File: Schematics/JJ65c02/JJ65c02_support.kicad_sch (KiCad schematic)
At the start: 40 parts, among them J1 ATMega J1, J2 Barrel_Jack, J3 VIA2 PortB, J4 ATMega J2, J6 AudioJack2, SW1 RESET, U2 NE555, U3 74HC00, U4 FT234XD, U5 74AC138, U6 LM386, U7 LM2940T-5.0/LF08, U8 ATmega328P-P, X1 1Mhz, X2 1.8Mhz, Y1 16Mhz

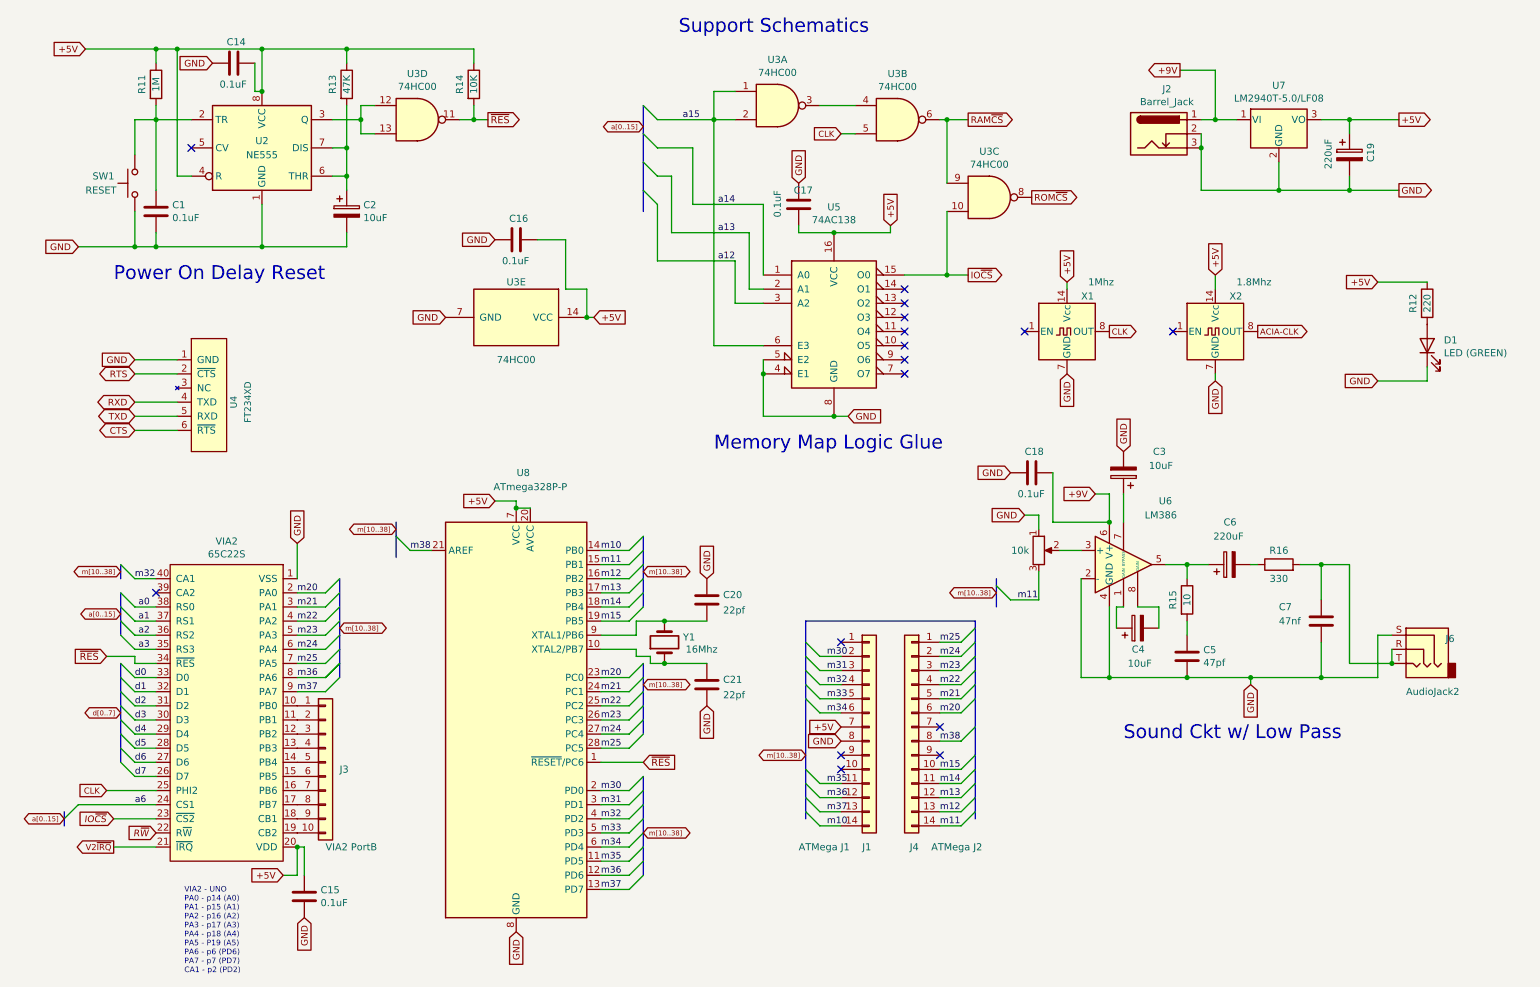
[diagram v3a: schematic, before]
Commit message: Refresh with current Schematics and wire-paths
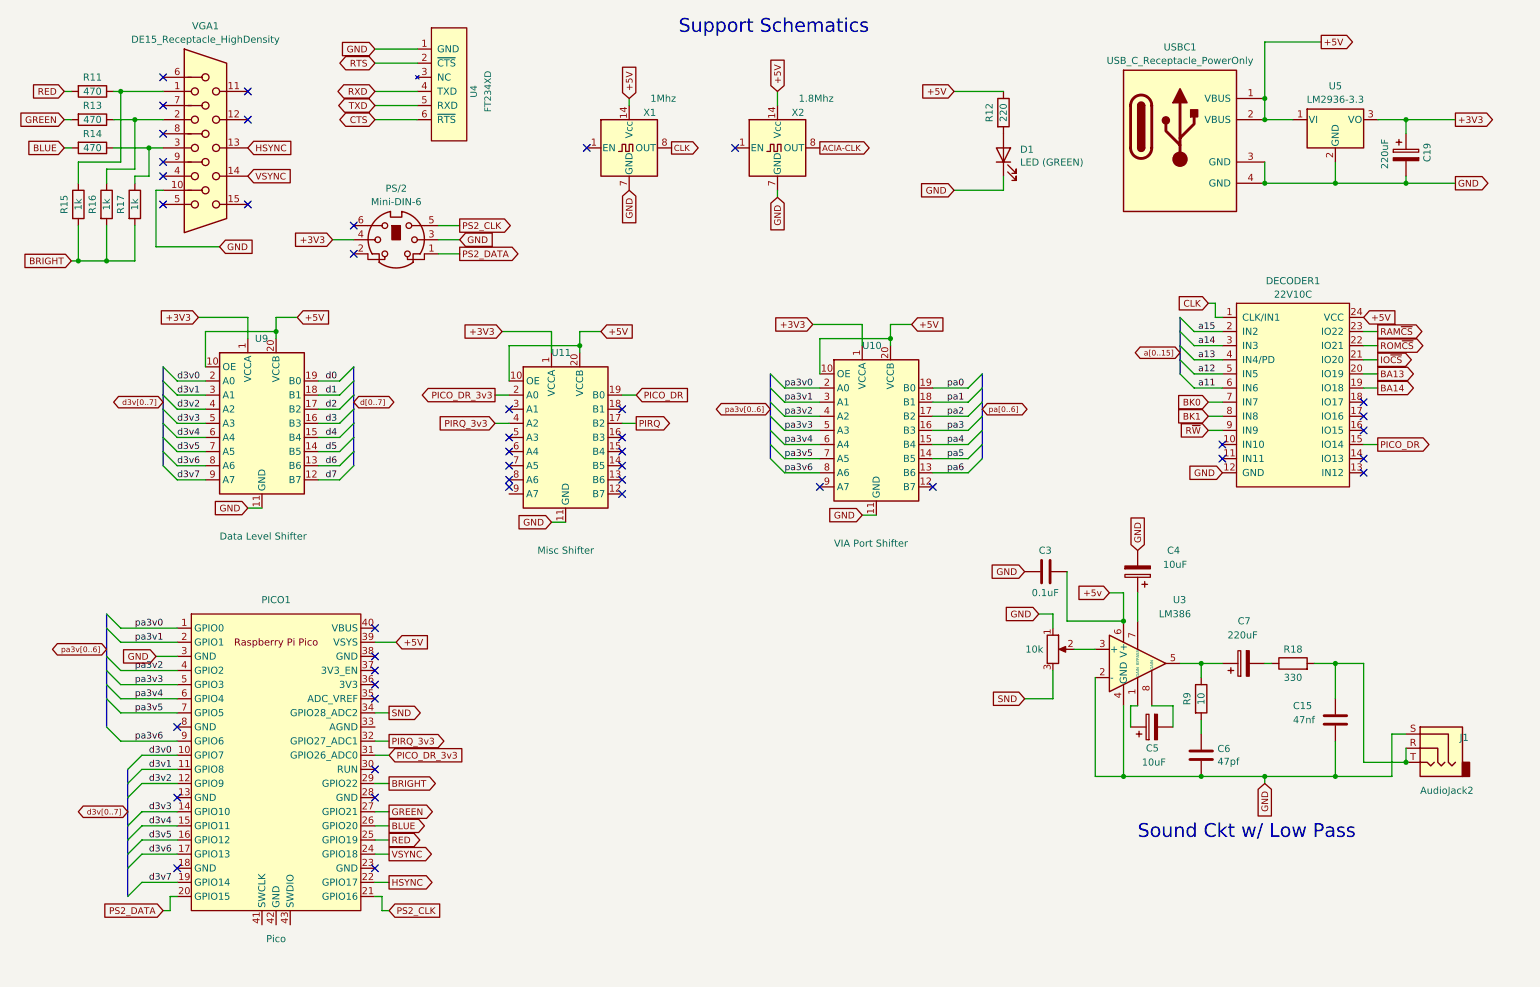
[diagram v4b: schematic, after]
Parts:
- removed C1, C14, C16, C17, C18: 0.1uF, Capacitor_THT:C_Disc_D4.7mm_W2.5mm_P5.00mm, symbol Device:C
- removed C2, C3: 10uF, Capacitor_THT:CP_Radial_D5.0mm_P2.50mm, symbol Device:C_Polarized
- removed C20, C21: 22pf, Capacitor_THT:C_Disc_D4.7mm_W2.5mm_P5.00mm, symbol Device:C
- removed C5: 47pf, Capacitor_THT:C_Disc_D4.7mm_W2.5mm_P5.00mm, symbol Device:C
- removed C6: 220uF, Capacitor_THT:CP_Radial_D6.3mm_P2.50mm, symbol Device:C_Polarized
- removed C7: 47nf, Capacitor_THT:C_Disc_D4.7mm_W2.5mm_P5.00mm, symbol Device:C
- removed J1: ATMega J1, Connector_PinHeader_2.54mm:PinHeader_1x14_P2.54mm_Vertical, symbol Connector_Generic:Conn_01x14
- removed J2: Barrel_Jack, Connector_BarrelJack:BarrelJack_Horizontal, symbol Connector:Barrel_Jack_Switch_Pin3Ring
- removed J3: VIA2 PortB, Connector_PinHeader_2.54mm:PinHeader_1x10_P2.54mm_Vertical, symbol Connector_Generic:Conn_01x10
- removed J4: ATMega J2, Connector_PinHeader_2.54mm:PinHeader_1x14_P2.54mm_Vertical, symbol Connector_Generic:Conn_01x14
- removed J6: AudioJack2, Connector_Audio:Jack_3.5mm_CUI_SJ1-3533NG_Horizontal, symbol Connector:AudioJack3
- removed RV2: 10k, Potentiometer_THT:Potentiometer_Bourns_3339P_Vertical, symbol Device:R_Potentiometer
- removed SW1: RESET, Button_Switch_THT:SW_PUSH_6mm, symbol Switch:SW_Push
- removed U2: NE555, Package_DIP:DIP-8_W7.62mm_Socket, symbol Timer:LM555xN
- removed U3: 74HC00, Package_DIP:DIP-14_W7.62mm_Socket, symbol 74xx:74HC00
- removed U5: 74AC138, Package_DIP:DIP-16_W7.62mm_Socket, symbol 74xx:74LS138
- removed U6: LM386, Package_DIP:DIP-8_W7.62mm_Socket, symbol Amplifier_Audio:LM386
- removed U7: LM2940T-5.0/LF08, Package_TO_SOT_THT:TO-262-3_Vertical, symbol JJ65c02-rescue:LM2940
- removed U8: ATmega328P-P, Package_DIP:DIP-28_W7.62mm_Socket, symbol MCU_Microchip_ATmega:ATmega328P-P
- removed VIA2: 65C22S, Package_DIP:DIP-40_W15.24mm_Socket, symbol 6502:65C22S
- removed Y1: 16Mhz, Crystal:Crystal_HC18-U_Vertical, symbol Device:Crystal
- added C3: 0.1uF, Capacitor_THT:C_Disc_D4.7mm_W2.5mm_P5.00mm, symbol Device:C
- added C5: 10uF, Capacitor_THT:CP_Radial_D5.0mm_P2.50mm, symbol Device:C_Polarized
- added C6: 47pf, Capacitor_THT:C_Disc_D4.7mm_W2.5mm_P5.00mm, symbol Device:C
- added C7: 220uF, Capacitor_THT:CP_Radial_D6.3mm_P2.50mm, symbol Device:C_Polarized
- added DECODER1: 22V10C, Package_DIP:DIP-24_W7.62mm_Socket, symbol 6502:22V10C
- added J1: AudioJack2, Connector_Audio:Jack_3.5mm_CUI_SJ1-3533NG_Horizontal, symbol Connector:AudioJack3
- added PICO1: Pico, JJ65c02:RPi_Pico_SMD_TH, symbol JJ65c02-rescue:Pico
- added PS/2: Mini-DIN-6, JJ65c02:mini_din-6, symbol Connector:Mini-DIN-6
- added R17: 1k, Resistor_THT:R_Axial_DIN0207_L6.3mm_D2.5mm_P7.62mm_Horizontal, symbol Device:R
- added R18: 330, Resistor_THT:R_Axial_DIN0207_L6.3mm_D2.5mm_P7.62mm_Horizontal, symbol Device:R
- added R9: 10, Resistor_THT:R_Axial_DIN0207_L6.3mm_D2.5mm_P7.62mm_Horizontal, symbol Device:R
- added RV1: 10k, Potentiometer_THT:Potentiometer_Bourns_3339P_Vertical, symbol Device:R_Potentiometer
- added U10: VIA Port Shifter, JJ65c02:TXB0108, symbol JJ65c02-rescue:FXMA108
- added U11: Misc Shifter, JJ65c02:TXB0108, symbol JJ65c02-rescue:FXMA108
- added U3: LM386, Package_DIP:DIP-8_W7.62mm_Socket, symbol Amplifier_Audio:LM386
- added U5: LM2936-3.3, Package_TO_SOT_THT:TO-220-3_Vertical, symbol Regulator_Linear:LM2936-3.3
- added U9: Data Level Shifter, JJ65c02:TXB0108, symbol JJ65c02-rescue:FXMA108
- added USBC1: USB_C_Receptacle_PowerOnly, JJ65c02:USBC_power, symbol Connector:USB_C_Receptacle_PowerOnly_6P
- added VGA1: DE15_Receptacle_HighDensity, JJ65c02:CONN_HDE15P_AMP, symbol Connector:DE15_Receptacle_HighDensity
- C15: value 0.1uF -> 47nf
- R11: value 1M -> 470
- R13: value 47K -> 470
- R14: value 10K -> 470
- R15: value 10 -> 1k
- R16: value 330 -> 1k
- U4: footprint JJ65c02:maxboard -> TerminalBlock_TE-Connectivity:TerminalBlock_TE_282834-6_1x06_P2.54mm_Horizontal
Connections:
- net +5V: now also DECODER1.24 (VCC), PICO1.39 (VSYS), U10.10 (OE), U10.20 (VCCB), U11.10 (OE), U11.20 (VCCB), U5.1 (VI), U9.10 (OE), U9.20 (VCCB), USBC1.1 (VBUS), USBC1.2 (VBUS); no longer C15.1, C19.1, R11.1, R13.1, R14.1
- net CLK: now also DECODER1.1 (CLK/IN1)
- net GND: now also C4.2, C3.2, C6.2, DECODER1.12 (GND), J1.S, PICO1.3 (GND), PS/2.3, RV1.1, U10.11 (GND), U11.11 (GND), U3.2 (-), U3.4 (GND), U5.2 (GND), U9.11 (GND), USBC1.3 (GND), USBC1.4 (GND), VGA1.10
- net IO~{CS}: now also DECODER1.21 (IO20)
- net RAM~{CS}: now also DECODER1.23 (IO22)
- net ROM~{CS}: now also DECODER1.22 (IO21)
- net R~{W}: now also DECODER1.9 (IN9)
- net a12: now also DECODER1.5 (IN5)
- net a13: now also DECODER1.4 (IN4/PD)
- net a14: now also DECODER1.3 (IN3)
- net a15: now also DECODER1.2 (IN2)
- net d0: now also U9.19 (B0)
- net d1: now also U9.18 (B1)
- net d2: now also U9.17 (B2)
- net d3: now also U9.16 (B3)
- net d4: now also U9.15 (B4)
- net d5: now also U9.14 (B5)
- net d6: now also U9.13 (B6)
- net d7: now also U9.12 (B7)
- net RED: now reaches R11.2
- net RED: now also PICO1.25 (GPIO19)
- net GREEN: now reaches R13.2
- net GREEN: now also PICO1.27 (GPIO21)
- net at R16.1: now also R13.1, VGA1.2
- net BRIGHT: now reaches R16.2
- net BRIGHT: now also R15.2, PICO1.29 (GPIO22), R17.2
- net at C4.1: now also U3.7 (BYPASS)
- net at R15.1: now also R11.1, VGA1.1
- net ~{RES} renamed BLUE
- net BLUE: now also PICO1.26 (GPIO20)
- new net: C7.2, R18.1
- new net: C15.1, J1.R, J1.T, R18.2
- new net: C6.1, R9.2
- new net: R14.1, R17.1, VGA1.3
- new net: C5.1, U3.1 (GAIN)
- new net: RV1.2, U3.3 (+)
- new net: C7.1, R9.1, U3.5
- new net: C5.2, U3.8 (GAIN)
- new net +3V3: C19.1, PS/2.4, U10.1 (VCCA), U11.1 (VCCA), U5.3 (VO), U9.1 (VCCA)
- new net +5v: C3.1, U3.6 (V+)
- new net BA13: DECODER1.20 (IO19)
- new net BA14: DECODER1.19 (IO18)
- new net BK0: DECODER1.7 (IN7)
- new net BK1: DECODER1.8 (IN8)
- new net HSYNC: PICO1.22 (GPIO17), VGA1.13
- new net PICO_DR: DECODER1.15 (IO14), U11.19 (B0)
- new net PICO_DR_3v3: PICO1.31 (GPIO26_ADC0), U11.2 (A0)
- new net PIRQ: U11.17 (B2)
- new net PIRQ_3v3: PICO1.32 (GPIO27_ADC1), U11.4 (A2)
- new net PS2_CLK: PICO1.21 (GPIO16), PS/2.5
- new net PS2_DATA: PICO1.20 (GPIO15), PS/2.1
- new net SND: PICO1.34 (GPIO28_ADC2), RV1.3
- new net VSYNC: PICO1.24 (GPIO18), VGA1.14
- new net a11: DECODER1.6 (IN6)
- new net d3v0: PICO1.10 (GPIO7), U9.2 (A0)
- new net d3v1: PICO1.11 (GPIO8), U9.3 (A1)
- new net d3v2: PICO1.12 (GPIO9), U9.4 (A2)
- new net d3v3: PICO1.14 (GPIO10), U9.5 (A3)
- new net d3v4: PICO1.15 (GPIO11), U9.6 (A4)
- new net d3v5: PICO1.16 (GPIO12), U9.7 (A5)
- new net d3v6: PICO1.17 (GPIO13), U9.8 (A6)
- new net d3v7: PICO1.19 (GPIO14), U9.9 (A7)
- new net pa0: U10.19 (B0)
- new net pa1: U10.18 (B1)
- new net pa2: U10.17 (B2)
- new net pa3: U10.16 (B3)
- new net pa3v0: PICO1.1 (GPIO0), U10.2 (A0)
- new net pa3v1: PICO1.2 (GPIO1), U10.3 (A1)
- new net pa3v2: PICO1.4 (GPIO2), U10.4 (A2)
- new net pa3v3: PICO1.5 (GPIO3), U10.5 (A3)
- new net pa3v4: PICO1.6 (GPIO4), U10.6 (A4)
- new net pa3v5: PICO1.7 (GPIO5), U10.7 (A5)
- new net pa3v6: PICO1.9 (GPIO6), U10.8 (A6)
- new net pa4: U10.15 (B4)
- new net pa5: U10.14 (B5)
- new net pa6: U10.13 (B6)
- no-connect marks 16 -> 45
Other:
- note removed: "Memory Map Logic Glue"
- note removed: "Power On Delay Reset"
- note removed: "VIA2 - UNO PA0 - p14 (A0) PA1 - p15 (A1) PA2 - p16 (A2) PA3 - p17 (A3) PA4 - p18 (A4) PA5 - P19 (A5) PA6 - p6 (PD6) PA7 - p7 (PD7) CA1 - p2 (PD2)"
- moved on the sheet: C19, D1, R12, U4, X1, X2

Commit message: Reorder RGB
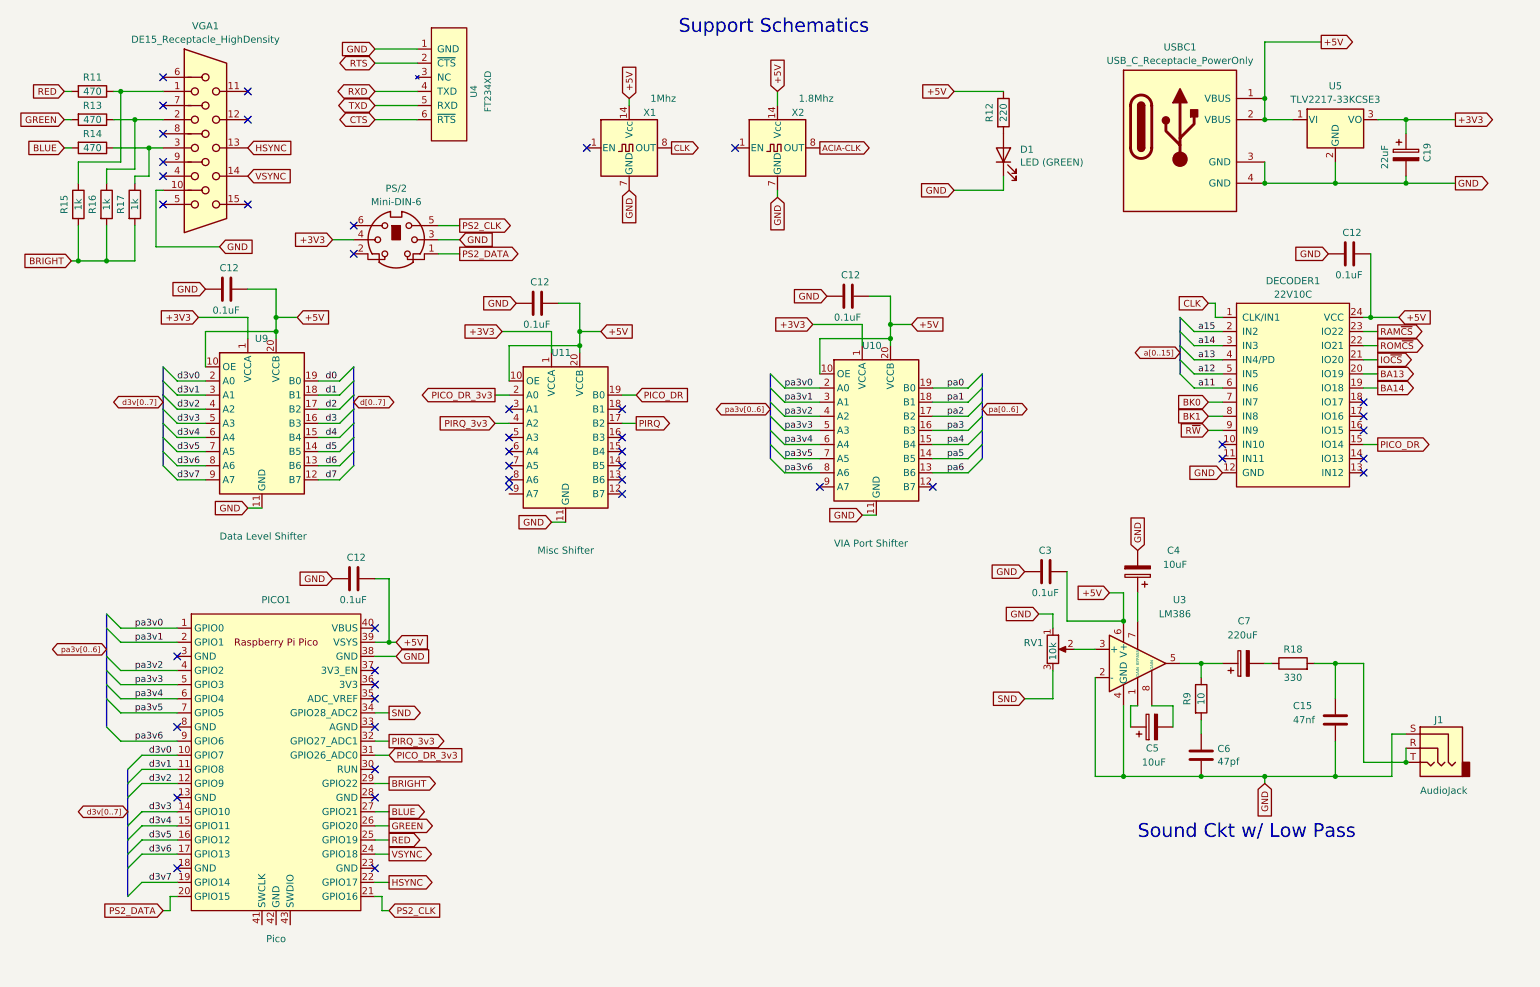
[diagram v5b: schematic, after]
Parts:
- added C12 (x5): 0.1uF, Capacitor_THT:C_Disc_D4.7mm_W2.5mm_P5.00mm, symbol Device:C
- C19: value 220uF -> 22uF
- J1: value AudioJack2 -> AudioJack
- U5: value LM2936-3.3 -> TLV2217-33KCSE3
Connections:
- net +5v is gone; now on net +5V: C3.1, U3.6 (V+)
- net +5V: now also C12.1, C12.1, C12.1, C12.1, C12.1
- net BLUE: now also PICO1.27 (GPIO21); no longer PICO1.26 (GPIO20)
- net GND: now also PICO1.38 (GND), C12.2, C12.2, C12.2, C12.2, C12.2; no longer PICO1.3 (GND)
- net GREEN: now also PICO1.26 (GPIO20); no longer PICO1.27 (GPIO21)
- no-connect marks 45 -> 46

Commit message: Latest version... ready for PCBs??
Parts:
- renumbered U3 to LM386, U4 to RS232
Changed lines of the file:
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@@
     (pin "4")
     (pin "40")
-    (pin "41")
-    (pin "42")
-    (pin "43")
     (pin "5")
     (pin "6")
@@
       (effects (font (size 1.27 1.27)))
     )
-    (property "Value" "330" (at 242.57 133.35 90)
+    (property "Value" "330" (at 242.57 130.81 90)
       (effects (font (size 1.27 1.27)))
     )
@@
   (symbol (lib_id "JJ65c02-rescue:FT234XD") (at 82.55 30.48 90) (unit 1)
     (in_bom yes) (on_board yes) (dnp no)
-    (property "Reference" "U4" (at 95.25 27.94 0)
+    (property "Reference" "RS232" (at 95.25 27.94 0)
       (effects (font (size 1.1938 1.1938)))
     )
@@
       (project "JJ65c02"
         (path "/2db910a0-b943-40b4-b81f-068ba5265f56/00000000-0000-0000-0000-000061660cac"
-          (reference "U4") (unit 1)
+          (reference "RS232") (unit 1)
         )
       )
@@
   (symbol (lib_id "Amplifier_Audio:LM386") (at 214.63 130.81 0) (unit 1)
     (in_bom yes) (on_board yes) (dnp no)
-    (property "Reference" "U3" (at 220.98 119.38 0)
+    (property "Reference" "LM386" (at 220.98 119.38 0)
       (effects (font (size 1.27 1.27)) (justify left))
     )
@@
       (project "JJ65c02"
         (path "/2db910a0-b943-40b4-b81f-068ba5265f56/00000000-0000-0000-0000-000061660cac"
-          (reference "U3") (unit 1)
-        )
-      )
+          (reference "LM386") (unit 1)
+        )
+      )
